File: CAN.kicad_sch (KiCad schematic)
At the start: 4 parts, among them U4 TJA1051T-3

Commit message: update
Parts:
- C24, C25: footprint Capacitor_SMD:C_0603_1608Metric -> Capacitor_SMD:C_0805_2012Metric
- R40: footprint Resistor_SMD:R_0603_1608Metric -> Resistor_SMD:R_0805_2012Metric
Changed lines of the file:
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@@
       (effects (font (size 1.27 1.27)) (justify left))
     )
-    (property "Footprint" "Capacitor_SMD:C_0603_1608Metric" (id 2) (at 94.9452 106.68 0)
+    (property "Footprint" "Capacitor_SMD:C_0805_2012Metric" (id 2) (at 94.9452 106.68 0)
       (effects (font (size 1.27 1.27)) hide)
     )
@@
       (effects (font (size 1.27 1.27)) (justify left))
     )
-    (property "Footprint" "Capacitor_SMD:C_0603_1608Metric" (id 2) (at 122.8852 80.01 0)
+    (property "Footprint" "Capacitor_SMD:C_0805_2012Metric" (id 2) (at 122.8852 80.01 0)
       (effects (font (size 1.27 1.27)) hide)
     )
@@
       (effects (font (size 1.27 1.27)) (justify left))
     )
-    (property "Footprint" "Resistor_SMD:R_0603_1608Metric" (id 2) (at 149.352 93.98 90)
+    (property "Footprint" "Resistor_SMD:R_0805_2012Metric" (id 2) (at 149.352 93.98 90)
       (effects (font (size 1.27 1.27)) hide)
     )

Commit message: routed most tracks
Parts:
- added C44: 1n, Capacitor_SMD:C_0805_2012Metric, symbol Device:C
- added R75: 56, Resistor_SMD:R_0805_2012Metric, symbol Device:R
- R40: value 220 -> 56; LCSC (none) -> C422823
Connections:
- net CAN_L: now also R75.2; no longer R40.2
- net GND: now also C44.2
- new net: C44.1, R40.2, R75.1
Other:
- moved on the sheet: R40
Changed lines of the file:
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@@
   (junction (at 93.98 96.52) (diameter 0) (color 0 0 0 0)
   )
-  (junction (at 151.13 101.6) (diameter 0) (color 0 0 0 0)
+  (junction (at 151.13 93.98) (diameter 0) (color 0 0 0 0)
   )
   (junction (at 127 71.12) (diameter 0) (color 0 0 0 0)
   )
-  (junction (at 151.13 86.36) (diameter 0) (color 0 0 0 0)
+  (junction (at 151.13 109.22) (diameter 0) (color 0 0 0 0)
+  )
+  (junction (at 151.13 78.74) (diameter 0) (color 0 0 0 0)
   )
   (junction (at 106.68 109.22) (diameter 0) (color 0 0 0 0)
@@
     (stroke (width 0) (type default) (color 0 0 0 0))
   )
-  (wire (pts (xy 144.78 86.36) (xy 151.13 86.36))
-    (stroke (width 0) (type default) (color 0 0 0 0))
-  )
-  (wire (pts (xy 144.78 91.44) (xy 144.78 86.36))
+  (wire (pts (xy 151.13 88.9) (xy 151.13 93.98))
+    (stroke (width 0) (type default) (color 0 0 0 0))
+  )
+  (wire (pts (xy 161.29 102.87) (xy 161.29 104.14))
+    (stroke (width 0) (type default) (color 0 0 0 0))
+  )
+  (wire (pts (xy 144.78 78.74) (xy 151.13 78.74))
+    (stroke (width 0) (type default) (color 0 0 0 0))
+  )
+  (wire (pts (xy 144.78 91.44) (xy 144.78 78.74))
     (stroke (width 0) (type default) (color 0 0 0 0))
   )
@@
     (stroke (width 0) (type default) (color 0 0 0 0))
   )
+  (wire (pts (xy 151.13 93.98) (xy 161.29 93.98))
+    (stroke (width 0) (type default) (color 0 0 0 0))
+  )
   (wire (pts (xy 93.98 109.22) (xy 93.98 111.76))
     (stroke (width 0) (type default) (color 0 0 0 0))
@@
     (stroke (width 0) (type default) (color 0 0 0 0))
   )
+  (wire (pts (xy 151.13 105.41) (xy 151.13 109.22))
+    (stroke (width 0) (type default) (color 0 0 0 0))
+  )
+  (wire (pts (xy 151.13 93.98) (xy 151.13 97.79))
+    (stroke (width 0) (type default) (color 0 0 0 0))
+  )
   (wire (pts (xy 127 104.14) (xy 127 109.22))
     (stroke (width 0) (type default) (color 0 0 0 0))
   )
-  (wire (pts (xy 144.78 101.6) (xy 151.13 101.6))
-    (stroke (width 0) (type default) (color 0 0 0 0))
-  )
-  (wire (pts (xy 162.56 96.52) (xy 158.75 96.52))
+  (wire (pts (xy 144.78 109.22) (xy 151.13 109.22))
     (stroke (width 0) (type default) (color 0 0 0 0))
   )
@@
     (stroke (width 0) (type default) (color 0 0 0 0))
   )
-  (wire (pts (xy 151.13 86.36) (xy 151.13 90.17))
-    (stroke (width 0) (type default) (color 0 0 0 0))
-  )
-  (wire (pts (xy 158.75 91.44) (xy 158.75 86.36))
+  (wire (pts (xy 151.13 78.74) (xy 151.13 81.28))
+    (stroke (width 0) (type default) (color 0 0 0 0))
+  )
+  (wire (pts (xy 151.13 109.22) (xy 163.83 109.22))
     (stroke (width 0) (type default) (color 0 0 0 0))
   )
@@
     (stroke (width 0) (type default) (color 0 0 0 0))
   )
-  (wire (pts (xy 158.75 86.36) (xy 151.13 86.36))
+  (wire (pts (xy 151.13 78.74) (xy 162.56 78.74))
+    (stroke (width 0) (type default) (color 0 0 0 0))
+  )
+  (wire (pts (xy 161.29 95.25) (xy 161.29 93.98))
     (stroke (width 0) (type default) (color 0 0 0 0))
   )
@@
     (stroke (width 0) (type default) (color 0 0 0 0))
   )
-  (wire (pts (xy 158.75 96.52) (xy 158.75 101.6))
-    (stroke (width 0) (type default) (color 0 0 0 0))
-  )
   (wire (pts (xy 114.3 96.52) (xy 93.98 96.52))
     (stroke (width 0) (type default) (color 0 0 0 0))
   )
-  (wire (pts (xy 158.75 101.6) (xy 151.13 101.6))
-    (stroke (width 0) (type default) (color 0 0 0 0))
-  )
   (wire (pts (xy 93.98 96.52) (xy 93.98 99.06))
     (stroke (width 0) (type default) (color 0 0 0 0))
@@
     (stroke (width 0) (type default) (color 0 0 0 0))
   )
-  (wire (pts (xy 151.13 101.6) (xy 151.13 97.79))
-    (stroke (width 0) (type default) (color 0 0 0 0))
-  )
-  (wire (pts (xy 144.78 96.52) (xy 144.78 101.6))
+  (wire (pts (xy 144.78 96.52) (xy 144.78 109.22))
     (stroke (width 0) (type default) (color 0 0 0 0))
   )
   (wire (pts (xy 121.92 72.39) (xy 121.92 71.12))
-    (stroke (width 0) (type default) (color 0 0 0 0))
-  )
-  (wire (pts (xy 162.56 91.44) (xy 158.75 91.44))
     (stroke (width 0) (type default) (color 0 0 0 0))
   )
@@
     (effects (font (size 1.27 1.27)) (justify right))
   )
-  (hierarchical_label "CAN_L" (shape input) (at 162.56 96.52 0)
+  (hierarchical_label "CAN_L" (shape input) (at 163.83 109.22 0)
     (effects (font (size 1.27 1.27)) (justify left))
   )
-  (hierarchical_label "CAN_H" (shape input) (at 162.56 91.44 0)
+  (hierarchical_label "CAN_H" (shape input) (at 162.56 78.74 0)
     (effects (font (size 1.27 1.27)) (justify left))
   )
@@
   (symbol (lib_id "Device:C") (at 93.98 102.87 0) (unit 1)
     (in_bom yes) (on_board yes)
-    (property "Reference" "C24" (id 0) (at 88.9 101.6 0)
+    (property "Reference" "C24" (id 0) (at 87.63 100.33 0)
       (effects (font (size 1.27 1.27)) (justify left))
     )
@@
   (symbol (lib_id "Device:C") (at 121.92 76.2 0) (unit 1)
     (in_bom yes) (on_board yes)
-    (property "Reference" "C25" (id 0) (at 116.84 74.93 0)
+    (property "Reference" "C25" (id 0) (at 115.57 73.66 0)
       (effects (font (size 1.27 1.27)) (justify left))
     )
@@
     (pin "1")
     (pin "2")
+  )
+  (symbol (lib_id "power:GND") (at 161.29 104.14 0) (unit 1)
+    (in_bom yes) (on_board yes)
+    (property "Reference" "#PWR0133" (id 0) (at 161.29 110.49 0)
+      (effects (font (size 1.27 1.27)) hide)
+    )
+    (property "Value" "GND" (id 1) (at 157.48 106.68 0))
+    (property "Footprint" "" (id 2) (at 161.29 104.14 0)
+      (effects (font (size 1.27 1.27)) hide)
+    )
+    (property "Datasheet" "" (id 3) (at 161.29 104.14 0)
+      (effects (font (size 1.27 1.27)) hide)
+    )
+    (pin "1")
   )
   (symbol (lib_id "power:+3V3") (at 93.98 92.71 0) (unit 1)
@@
     (pin "1")
   )
-  (symbol (lib_id "Device:R") (at 151.13 93.98 0) (unit 1)
-    (in_bom yes) (on_board yes) (fields_autoplaced)
-    (property "Reference" "R40" (id 0) (at 153.67 92.7099 0)
-      (effects (font (size 1.27 1.27)) (justify left))
-    )
-    (property "Value" "220" (id 1) (at 153.67 95.2499 0)
-      (effects (font (size 1.27 1.27)) (justify left))
-    )
-    (property "Footprint" "Resistor_SMD:R_0805_2012Metric" (id 2) (at 149.352 93.98 90)
-      (effects (font (size 1.27 1.27)) hide)
-    )
-    (property "Datasheet" "~" (id 3) (at 151.13 93.98 0)
+  (symbol (lib_id "Device:R") (at 151.13 101.6 0) (unit 1)
+    (in_bom yes) (on_board yes) (fields_autoplaced)
+    (property "Reference" "R75" (id 0) (at 153.67 100.3299 0)
+      (effects (font (size 1.27 1.27)) (justify left))
+    )
+    (property "Value" "56" (id 1) (at 153.67 102.8699 0)
+      (effects (font (size 1.27 1.27)) (justify left))
+    )
+    (property "Footprint" "Resistor_SMD:R_0805_2012Metric" (id 2) (at 149.352 101.6 90)
+      (effects (font (size 1.27 1.27)) hide)
+    )
+    (property "Datasheet" "~" (id 3) (at 151.13 101.6 0)
+      (effects (font (size 1.27 1.27)) hide)
+    )
+    (property "LCSC" "C422823" (id 4) (at 151.13 101.6 0)
+      (effects (font (size 1.27 1.27)) hide)
+    )
+    (pin "1")
+    (pin "2")
+  )
+  (symbol (lib_id "Device:R") (at 151.13 85.09 0) (unit 1)
+    (in_bom yes) (on_board yes) (fields_autoplaced)
+    (property "Reference" "R40" (id 0) (at 153.67 83.8199 0)
+      (effects (font (size 1.27 1.27)) (justify left))
+    )
+    (property "Value" "56" (id 1) (at 153.67 86.3599 0)
+      (effects (font (size 1.27 1.27)) (justify left))
+    )
+    (property "Footprint" "Resistor_SMD:R_0805_2012Metric" (id 2) (at 149.352 85.09 90)
+      (effects (font (size 1.27 1.27)) hide)
+    )
+    (property "Datasheet" "~" (id 3) (at 151.13 85.09 0)
+      (effects (font (size 1.27 1.27)) hide)
+    )
+    (property "LCSC" "C422823" (id 4) (at 151.13 85.09 0)
       (effects (font (size 1.27 1.27)) hide)
     )
@@
     (pin "1")
   )
+  (symbol (lib_id "Device:C") (at 161.29 99.06 0) (unit 1)
+    (in_bom yes) (on_board yes) (fields_autoplaced)
+    (property "Reference" "C44" (id 0) (at 165.1 97.7899 0)
+      (effects (font (size 1.27 1.27)) (justify left))
+    )
+    (property "Value" "1n" (id 1) (at 165.1 100.3299 0)
+      (effects (font (size 1.27 1.27)) (justify left))
+    )
+    (property "Footprint" "Capacitor_SMD:C_0805_2012Metric" (id 2) (at 162.2552 102.87 0)
+      (effects (font (size 1.27 1.27)) hide)
+    )
+    (property "Datasheet" "~" (id 3) (at 161.29 99.06 0)
+      (effects (font (size 1.27 1.27)) hide)
+    )
+    (property "LCSC" "C440004" (id 4) (at 161.29 99.06 0)
+      (effects (font (size 1.27 1.27)) hide)
+    )
+    (pin "1")
+    (pin "2")
+  )
 )

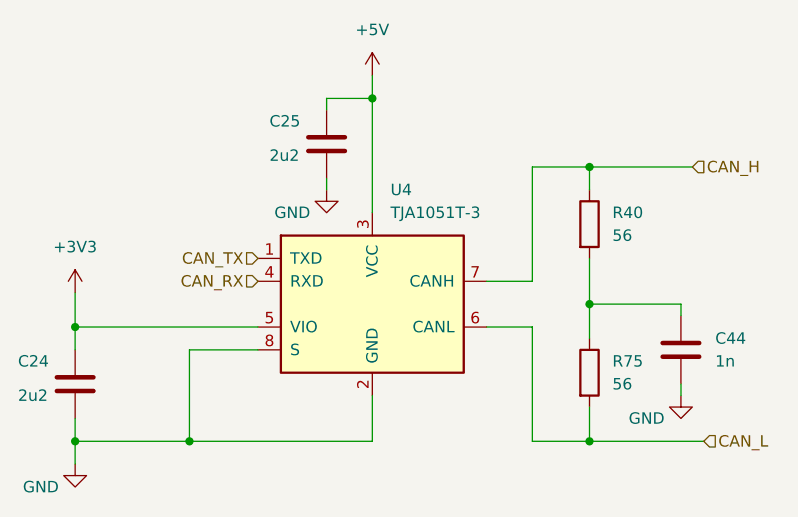
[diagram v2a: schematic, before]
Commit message: new board dimensions
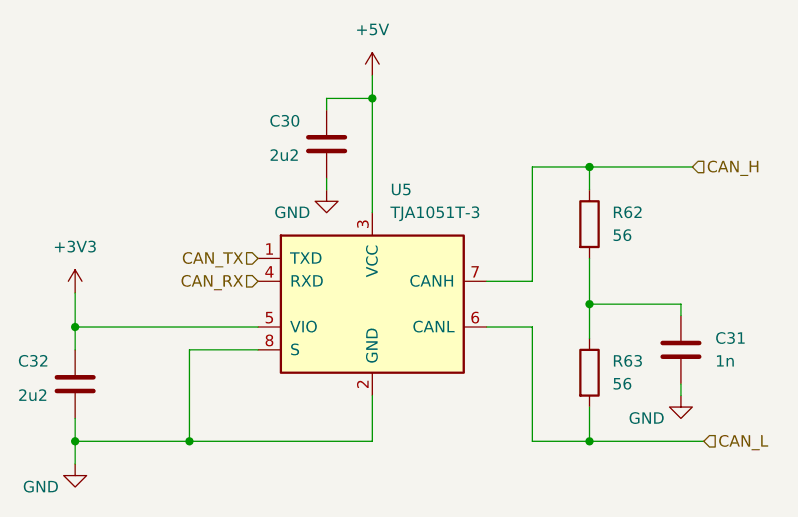
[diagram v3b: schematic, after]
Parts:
- R62: renamed from R40; LCSC C422823 -> C17757
- U5: renamed from U4; LCSC (none) -> c58988
- renumbered C25 to C30, C44 to C31, C24 to C32, R75 to R63
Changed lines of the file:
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@@
   (symbol (lib_id "power:+5V") (at 127 68.58 0) (unit 1)
     (in_bom yes) (on_board yes) (fields_autoplaced)
-    (property "Reference" "#PWR06" (id 0) (at 127 72.39 0)
+    (property "Reference" "#PWR029" (id 0) (at 127 72.39 0)
       (effects (font (size 1.27 1.27)) hide)
     )
@@
   (symbol (lib_id "power:GND") (at 121.92 81.28 0) (unit 1)
     (in_bom yes) (on_board yes)
-    (property "Reference" "#PWR05" (id 0) (at 121.92 87.63 0)
+    (property "Reference" "#PWR030" (id 0) (at 121.92 87.63 0)
       (effects (font (size 1.27 1.27)) hide)
     )
@@
   (symbol (lib_id "Device:C") (at 93.98 102.87 0) (unit 1)
     (in_bom yes) (on_board yes)
-    (property "Reference" "C24" (id 0) (at 87.63 100.33 0)
+    (property "Reference" "C32" (id 0) (at 87.63 100.33 0)
       (effects (font (size 1.27 1.27)) (justify left))
     )
@@
   (symbol (lib_id "Interface_CAN_LIN:TJA1051T-3") (at 127 93.98 0) (unit 1)
     (in_bom yes) (on_board yes) (fields_autoplaced)
-    (property "Reference" "U4" (id 0) (at 129.0194 81.28 0)
+    (property "Reference" "U5" (id 0) (at 129.0194 81.28 0)
       (effects (font (size 1.27 1.27)) (justify left))
     )
@@
     )
     (property "Datasheet" "http://www.nxp.com/documents/data_sheet/TJA1051.pdf" (id 3) (at 127 93.98 0)
+      (effects (font (size 1.27 1.27)) hide)
+    )
+    (property "LCSC" "c58988" (id 4) (at 127 93.98 0)
       (effects (font (size 1.27 1.27)) hide)
     )
@@
   (symbol (lib_id "Device:C") (at 121.92 76.2 0) (unit 1)
     (in_bom yes) (on_board yes)
-    (property "Reference" "C25" (id 0) (at 115.57 73.66 0)
+    (property "Reference" "C30" (id 0) (at 115.57 73.66 0)
       (effects (font (size 1.27 1.27)) (justify left))
     )
@@
   (symbol (lib_id "power:GND") (at 161.29 104.14 0) (unit 1)
     (in_bom yes) (on_board yes)
-    (property "Reference" "#PWR0133" (id 0) (at 161.29 110.49 0)
+    (property "Reference" "#PWR032" (id 0) (at 161.29 110.49 0)
       (effects (font (size 1.27 1.27)) hide)
     )
@@
   (symbol (lib_id "power:+3V3") (at 93.98 92.71 0) (unit 1)
     (in_bom yes) (on_board yes) (fields_autoplaced)
-    (property "Reference" "#PWR03" (id 0) (at 93.98 96.52 0)
+    (property "Reference" "#PWR031" (id 0) (at 93.98 96.52 0)
       (effects (font (size 1.27 1.27)) hide)
     )
@@
   (symbol (lib_id "Device:R") (at 151.13 101.6 0) (unit 1)
     (in_bom yes) (on_board yes) (fields_autoplaced)
-    (property "Reference" "R75" (id 0) (at 153.67 100.3299 0)
+    (property "Reference" "R63" (id 0) (at 153.67 100.3299 0)
       (effects (font (size 1.27 1.27)) (justify left))
     )
@@
   (symbol (lib_id "Device:R") (at 151.13 85.09 0) (unit 1)
     (in_bom yes) (on_board yes) (fields_autoplaced)
-    (property "Reference" "R40" (id 0) (at 153.67 83.8199 0)
+    (property "Reference" "R62" (id 0) (at 153.67 83.8199 0)
       (effects (font (size 1.27 1.27)) (justify left))
     )
@@
       (effects (font (size 1.27 1.27)) hide)
     )
-    (property "LCSC" "C422823" (id 4) (at 151.13 85.09 0)
+    (property "LCSC" "C17757" (id 4) (at 151.13 85.09 0)
       (effects (font (size 1.27 1.27)) hide)
     )
@@
   (symbol (lib_id "power:GND") (at 93.98 111.76 0) (unit 1)
     (in_bom yes) (on_board yes)
-    (property "Reference" "#PWR04" (id 0) (at 93.98 118.11 0)
+    (property "Reference" "#PWR033" (id 0) (at 93.98 118.11 0)
       (effects (font (size 1.27 1.27)) hide)
     )
@@
   (symbol (lib_id "Device:C") (at 161.29 99.06 0) (unit 1)
     (in_bom yes) (on_board yes) (fields_autoplaced)
-    (property "Reference" "C44" (id 0) (at 165.1 97.7899 0)
+    (property "Reference" "C31" (id 0) (at 165.1 97.7899 0)
       (effects (font (size 1.27 1.27)) (justify left))
     )
